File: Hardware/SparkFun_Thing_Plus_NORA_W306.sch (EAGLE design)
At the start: 72 parts, among them J1 THING_PLUS_LOGICAL, J2 LiPo, J3 QWIIC_RA, J4 MICRO-SDFRICTION, J5 USB-C, J6 SWD (DNP), Q1 3.1A/30V/105mΩ, Q2 MBT3904DW1T1, U1 UBLOX_NORA_W306, U3 XC6222B331MR-G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

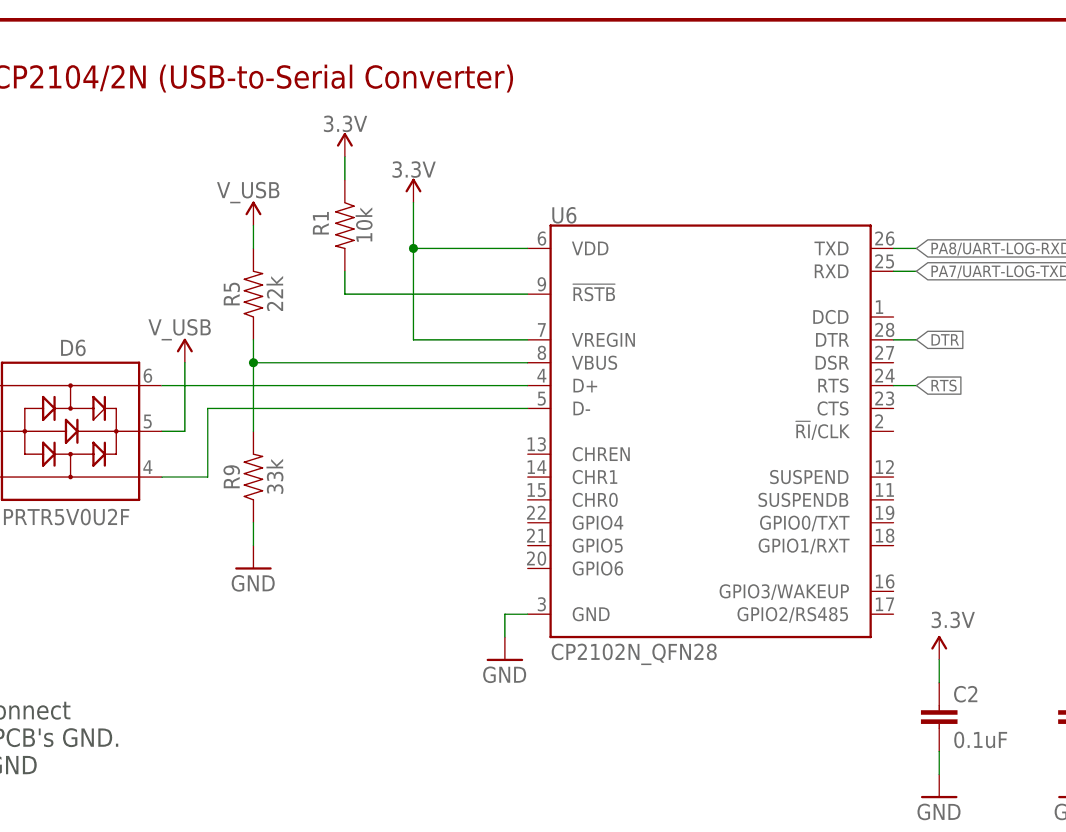
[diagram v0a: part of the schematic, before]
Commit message: Switched CP2102 to QFN24 package type
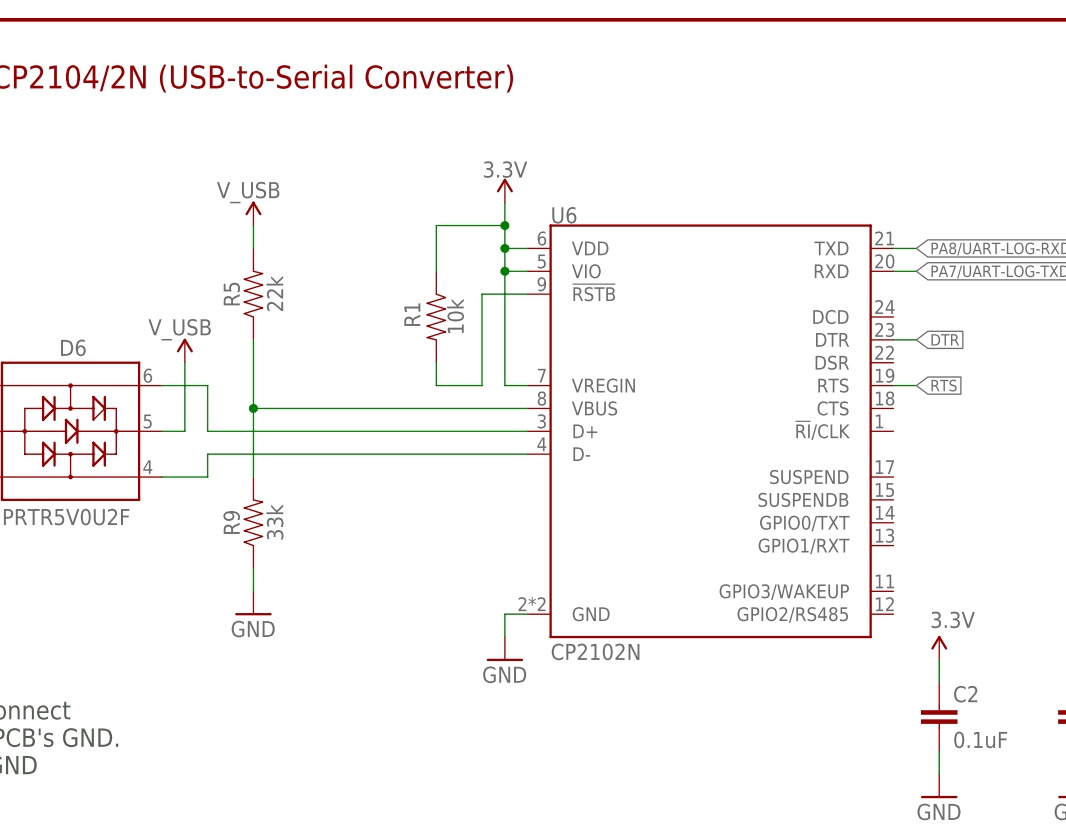
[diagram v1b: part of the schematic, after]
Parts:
- U6: value CP2102N_QFN28 -> CP2102N; device nora-w306:CP2102N_QFN28 -> SparkFun-IC-Comms:CP2102N
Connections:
- net 3.3V: now also U6.VIO
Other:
- moved on the sheet: R1, R9
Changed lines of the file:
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@@
 <part name="GND31" library="SparkFun-PowerSymbols" deviceset="GND" device=""/>
 <part name="CHG" library="SparkFun-Jumpers" deviceset="JUMPER-SMT_2_NC_TRACE" device="_SILK" package3d_urn="urn:adsk.eagle:package:39281/1" value=""/>
-<part name="U6" library="nora-w306" deviceset="CP2102N_QFN28" device=""/>
+<part name="U6" library="SparkFun-IC-Comms" deviceset="CP2102N" device=""/>
 <part name="GND32" library="SparkFun-PowerSymbols" deviceset="GND" device=""/>
-<part name="SUPPLY29" library="SparkFun-PowerSymbols" deviceset="3.3V" device=""/>
 <part name="JP3" library="SparkFun-Jumpers" deviceset="JUMPER-SMT_2_NC_TRACE" device="_SILK" package3d_urn="urn:adsk.eagle:package:39281/1" value=""/>
 <part name="I2C" library="SparkFun-Jumpers" deviceset="JUMPER-SMT_3_2-NC_TRACE" device="_SILK" package3d_urn="urn:adsk.eagle:package:39289/1"/>
@@
 <attribute name="VALUE" x="373.38" y="132.08" size="1.778" layer="96" font="vector"/>
 </instance>
-<instance part="R1" gate="G$1" x="340.36" y="256.54" smashed="yes" rot="R270">
-<attribute name="NAME" x="336.804" y="256.794" size="1.778" layer="95" font="vector" rot="R270" align="bottom-center"/>
-<attribute name="VALUE" x="343.408" y="256.54" size="1.778" layer="96" font="vector" rot="R270" align="top-center"/>
-</instance>
-<instance part="SUPPLY9" gate="G$1" x="347.98" y="259.08" smashed="yes">
-<attribute name="VALUE" x="347.98" y="261.874" size="1.778" layer="96" font="vector" align="bottom-center"/>
+<instance part="R1" gate="G$1" x="350.52" y="246.38" smashed="yes" rot="R270">
+<attribute name="NAME" x="346.964" y="246.634" size="1.778" layer="95" font="vector" rot="R270" align="bottom-center"/>
+<attribute name="VALUE" x="353.568" y="246.38" size="1.778" layer="96" font="vector" rot="R270" align="top-center"/>
+</instance>
+<instance part="SUPPLY9" gate="G$1" x="358.14" y="259.08" smashed="yes">
+<attribute name="VALUE" x="358.14" y="261.874" size="1.778" layer="96" font="vector" align="bottom-center"/>
 </instance>
 <instance part="SUPPLY3" gate="G$1" x="167.64" y="165.1" smashed="yes" rot="MR0">
@@
 <attribute name="VALUE" x="331.724" y="248.92" size="1.778" layer="96" font="vector" rot="R90" align="top-center"/>
 </instance>
-<instance part="R9" gate="G$1" x="330.2" y="228.6" smashed="yes" rot="R90">
-<attribute name="NAME" x="328.676" y="228.6" size="1.778" layer="95" font="vector" rot="R90" align="bottom-center"/>
-<attribute name="VALUE" x="331.724" y="228.6" size="1.778" layer="96" font="vector" rot="R90" align="top-center"/>
-</instance>
-<instance part="GND3" gate="1" x="330.2" y="218.44" smashed="yes">
-<attribute name="VALUE" x="327.66" y="215.9" size="1.778" layer="96" font="vector"/>
+<instance part="R9" gate="G$1" x="330.2" y="223.52" smashed="yes" rot="R90">
+<attribute name="NAME" x="328.676" y="223.52" size="1.778" layer="95" font="vector" rot="R90" align="bottom-center"/>
+<attribute name="VALUE" x="331.724" y="223.52" size="1.778" layer="96" font="vector" rot="R90" align="top-center"/>
+</instance>
+<instance part="GND3" gate="1" x="330.2" y="213.36" smashed="yes">
+<attribute name="VALUE" x="327.66" y="210.82" size="1.778" layer="96" font="vector"/>
 </instance>
 <instance part="C2" gate="G$1" x="406.4" y="200.66" smashed="yes">
@@
 <instance part="GND32" gate="1" x="358.14" y="208.28" smashed="yes">
 <attribute name="VALUE" x="355.6" y="205.74" size="1.778" layer="96" font="vector"/>
-</instance>
-<instance part="SUPPLY29" gate="G$1" x="340.36" y="264.16" smashed="yes">
-<attribute name="VALUE" x="340.36" y="266.954" size="1.778" layer="96" font="vector" align="bottom-center"/>
 </instance>
 <instance part="JP3" gate="G$1" x="170.18" y="60.96" smashed="yes">
@@
 </segment>
 <segment>
-<pinref part="SUPPLY29" gate="G$1" pin="3.3V"/>
+<pinref part="SUPPLY9" gate="G$1" pin="3.3V"/>
+<junction x="358.14" y="254"/>
+<wire x1="358.14" y1="238.76" x2="358.14" y2="251.46" width="0.1524" layer="91"/>
+<wire x1="358.14" y1="251.46" x2="358.14" y2="254" width="0.1524" layer="91"/>
+<wire x1="358.14" y1="254" x2="358.14" y2="256.54" width="0.1524" layer="91"/>
+<pinref part="U6" gate="G$1" pin="VDD"/>
+<wire x1="358.14" y1="256.54" x2="358.14" y2="259.08" width="0.1524" layer="91"/>
+<wire x1="358.14" y1="254" x2="360.68" y2="254" width="0.1524" layer="91"/>
+<pinref part="U6" gate="G$1" pin="VREGIN"/>
+<wire x1="358.14" y1="238.76" x2="360.68" y2="238.76" width="0.1524" layer="91"/>
 <pinref part="R1" gate="G$1" pin="1"/>
-<wire x1="340.36" y1="261.62" x2="340.36" y2="264.16" width="0.1524" layer="91"/>
-</segment>
-<segment>
-<pinref part="SUPPLY9" gate="G$1" pin="3.3V"/>
-<junction x="347.98" y="254"/>
-<wire x1="347.98" y1="243.84" x2="347.98" y2="254" width="0.1524" layer="91"/>
-<wire x1="347.98" y1="254" x2="347.98" y2="259.08" width="0.1524" layer="91"/>
-<pinref part="U6" gate="G$1" pin="VDD"/>
-<wire x1="347.98" y1="254" x2="360.68" y2="254" width="0.1524" layer="91"/>
-<pinref part="U6" gate="G$1" pin="VREGIN"/>
-<wire x1="347.98" y1="243.84" x2="360.68" y2="243.84" width="0.1524" layer="91"/>
+<wire x1="350.52" y1="251.46" x2="350.52" y2="256.54" width="0.1524" layer="91"/>
+<wire x1="358.14" y1="256.54" x2="350.52" y2="256.54" width="0.1524" layer="91"/>
+<junction x="358.14" y="256.54"/>
+<pinref part="U6" gate="G$1" pin="VIO"/>
+<wire x1="360.68" y1="251.46" x2="358.14" y2="251.46" width="0.1524" layer="91"/>
+<junction x="358.14" y="251.46"/>
 </segment>
 <segment>
@@
 <segment>
 <pinref part="R9" gate="G$1" pin="1"/>
-<wire x1="330.2" y1="223.52" x2="330.2" y2="220.98" width="0.1524" layer="91"/>
+<wire x1="330.2" y1="218.44" x2="330.2" y2="215.9" width="0.1524" layer="91"/>
 <pinref part="GND3" gate="1" pin="GND"/>
 </segment>
@@
 <segment>
 <pinref part="R1" gate="G$1" pin="2"/>
-<wire x1="340.36" y1="248.92" x2="340.36" y2="251.46" width="0.1524" layer="91"/>
+<wire x1="355.6" y1="238.76" x2="350.52" y2="238.76" width="0.1524" layer="91"/>
+<wire x1="350.52" y1="238.76" x2="350.52" y2="241.3" width="0.1524" layer="91"/>
 <pinref part="U6" gate="G$1" pin="!RSTB"/>
-<wire x1="340.36" y1="248.92" x2="360.68" y2="248.92" width="0.1524" layer="91"/>
+<wire x1="355.6" y1="238.76" x2="355.6" y2="248.92" width="0.1524" layer="91"/>
+<wire x1="355.6" y1="248.92" x2="360.68" y2="248.92" width="0.1524" layer="91"/>
 </segment>
 </net>
@@
 <pinref part="R9" gate="G$1" pin="2"/>
 <pinref part="R5" gate="G$1" pin="1"/>
-<wire x1="330.2" y1="233.68" x2="330.2" y2="241.3" width="0.1524" layer="91"/>
-<wire x1="330.2" y1="241.3" x2="330.2" y2="243.84" width="0.1524" layer="91"/>
-<junction x="330.2" y="241.3"/>
-<wire x1="360.68" y1="241.3" x2="330.2" y2="241.3" width="0.1524" layer="91"/>
+<wire x1="330.2" y1="228.6" x2="330.2" y2="236.22" width="0.1524" layer="91"/>
+<wire x1="330.2" y1="236.22" x2="330.2" y2="243.84" width="0.1524" layer="91"/>
+<junction x="330.2" y="236.22"/>
+<wire x1="360.68" y1="236.22" x2="330.2" y2="236.22" width="0.1524" layer="91"/>
 <pinref part="U6" gate="G$1" pin="VBUS"/>
 </segment>
@@
 <net name="N$15" class="0">
 <segment>
-<wire x1="360.68" y1="238.76" x2="320.04" y2="238.76" width="0.1524" layer="91"/>
+<wire x1="360.68" y1="233.68" x2="325.12" y2="233.68" width="0.1524" layer="91"/>
+<wire x1="325.12" y1="233.68" x2="325.12" y2="238.76" width="0.1524" layer="91"/>
+<wire x1="325.12" y1="238.76" x2="320.04" y2="238.76" width="0.1524" layer="91"/>
 <pinref part="D6" gate="D1" pin="6"/>
 <pinref part="U6" gate="G$1" pin="D+"/>
@@
 <net name="N$18" class="0">
 <segment>
-<wire x1="360.68" y1="236.22" x2="325.12" y2="236.22" width="0.1524" layer="91"/>
-<wire x1="325.12" y1="236.22" x2="325.12" y2="228.6" width="0.1524" layer="91"/>
+<wire x1="360.68" y1="231.14" x2="325.12" y2="231.14" width="0.1524" layer="91"/>
+<wire x1="325.12" y1="231.14" x2="325.12" y2="228.6" width="0.1524" layer="91"/>
 <wire x1="325.12" y1="228.6" x2="320.04" y2="228.6" width="0.1524" layer="91"/>
 <pinref part="D6" gate="D1" pin="4"/>

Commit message: Rerouted with new pin selections
-SPI0 now used for "main" SPI headers and uSD
-SPI1 PICO pin used for WS2812 control
-RX1/TX1 pins changed to other option on module
-I2C pins changed to other option on module
-SWD lines routed to DNP header on bottom side.
-most GPIOs switched/rerouted *note, Arduino pin map table not yet updated*
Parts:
- removed TP2: TEST-POINT3X5, SparkFun-Connectors:TEST-POINT3X5
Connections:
- removed net N$28: D5.DO, TP2.1
- removed net PA12/PICO: J1.PICO, J4.CMD/SDI, U1.PA12/LP_UART_TXD/SPI1_PICO/I2S_MCLK
- removed net PA13/POCI: J1.POCI, J4.DAT0/SDO, U1.PA13/LP_UART_RXD/SPI1_POCI/I2S_SD_TX1
- removed net PA14/SCK: J1.SCK, J4.CLK/SCK, U1.PA14/LP_UART_RTS/SPI1CLK/I2S_SD_TX2
- removed net PA15/CS: J1.A5, J4.DAT3/!CS!, U1.PA15/LP_UART_CTS/SPI1_CS
- removed net PA25/LP_UART_RXD: J1.RX, U1.PA25/HS_USI_SPI_PICO/HSDM/LP_UART_RXD
- removed net PA26/LP_UART_TXD: J1.TX, U1.PA26/HS_USI_SPI_POCI/HSDP/LP_UART_TXD
- removed net PB1: J1.A0, U1.PB1/LP_UART_TXD/ADC
- removed net PB18: J1.GPIO3, S3.1, S3.2, U1.PB18/HS_USI_USART0_RXD
- removed net PB19: J1.GPIO4, U1.PB19/HS_UART0_TXD/I2S_TX0
- removed net PB2: J1.A2, U1.PB2/LP_UART_RXD/PCM_CLK/ADC
- removed net PB20/SCL: J1.SCL, J3.4, R28.1, U1.PB20/HS_USI_I2C_SCL/I2S_CLK, U5.SCL
- removed net PB21/SDA: J1.SDA, J3.3, R29.1, U1.PB21/HS_USI_I2C_SDA/SPI0_CS/I2S_WS/QDEC_IDX, U5.SDA
- removed net PB3/ADC/SWD_CLK: J1.A1, J6.SWDCLK, U1.PB3/SWD_CLK/ADC
- new net PA12: J1.GPIO5, JP3.1, U1.PA12/LP_UART_TXD/SPI1_PICO/I2S_MCLK
- new net PA13: J1.GPIO6, U1.PA13/LP_UART_RXD/SPI1_POCI/I2S_SD_TX1
- new net PA14: J1.GPIO3, U1.PA14/LP_UART_RTS/SPI1_CLK/I2S_SD_TX2
- new net PA15: J1.GPIO4, U1.PA15/LP_UART_CTS/SPI1_CS
- new net PA25/SCL: J1.SCL, J3.4, R28.1, U1.PA25/LP_I2C_SCL/HSDM/LP_UART_RXD, U5.SCL
- new net PA26/SDA: J1.SDA, J3.3, R29.1, U1.PA26/LP_I2C_SDA/HSDP/LP_UART_TXD, U5.SDA
- new net PB1/LP_UART_TXD/A2: J1.TX, U1.PB1/LP_UART_TXD/ADC
- new net PB18/SPI0_PICO: J1.PICO, J4.CMD/SDI, U1.PB18/SPI0_PICO
- new net PB19/SPI0_POCI: J1.POCI, J4.DAT0/SDO, U1.PB19/SPI0_POCI/I2S_TX0
- new net PB2/LP_UART_RXD/A1: J1.RX, U1.PB2/LP_UART_RXD/PCM_CLK/ADC
- new net PB20/SPI0_CLK: J1.SCK, J4.CLK/SCK, U1.PB20/SPI0_CLK/I2S_CLK
- new net PB21/SPI0_CS: J1.A5, J4.DAT3/!CS!, U1.PB21/SPI0_CS/I2S_WS/QDEC_IDX
- new net PB3/SWD_CLK/A0: J1.A0, J6.SWDCLK, U1.PB3/SWD_CLK/ADC
- new net WS2812-DO: D5.DO, J1.GPIO0
- net PA28: now also J1.A4, U1.PA28/BT_CK/RREF; no longer J1.GPIO5, U1.PA28/HS_USI_SPI_CS/BT_CK/RREF
- net PA30: now also J1.A3, U1.PA30/HS_PWM7; no longer J1.GPIO6, U1.PA30/HS_USI_SPI_CLK/HS_PWM7
- net PA7/UART-LOG-TXD: now also J1.A2; no longer J1.A4
- net PA8/UART-LOG-RXD: now also J1.A1; no longer J1.A3
- net PB22: now also J1.GPIO1, JP4.1, S3.1, S3.2; no longer J1.GPIO2, JP3.1
- net PB23: now also J1.GPIO2; no longer J1.GPIO1, JP4.1
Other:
- note added: "Cut JP3 to disconnect mic data from GPIO pin."
- note removed: "Cut JP3 to disconnect mic data from D15"
- moved on the sheet: C8, U1

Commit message: Silk Labels updated
-and some minor layout tweaks
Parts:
- renumbered JP3 to JP1, JP4 to JP2
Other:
- note added: "***Boot Strap Pins*** (Include internal pull-ups) See DS PG 10 for more info. PA30 PB19/SWD_DATA PA7/UART-LOG-TXD"
- note removed: "***Boot Strap Pins*** (Include internal pull-ups) See DS PG 10 for more info. PA30 (D3/SCK) PB19/SWD_DATA (D13) PA7/UART-LOG-TXD (D1)"
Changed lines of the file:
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@@
 <part name="U6" library="SparkFun-IC-Comms" deviceset="CP2102N" device=""/>
 <part name="GND32" library="SparkFun-PowerSymbols" deviceset="GND" device=""/>
-<part name="JP3" library="SparkFun-Jumpers" deviceset="JUMPER-SMT_2_NC_TRACE" device="_SILK" package3d_urn="urn:adsk.eagle:package:39281/1" value=""/>
+<part name="JP1" library="SparkFun-Jumpers" deviceset="JUMPER-SMT_2_NC_TRACE" device="_SILK" package3d_urn="urn:adsk.eagle:package:39281/1" value=""/>
 <part name="I2C" library="SparkFun-Jumpers" deviceset="JUMPER-SMT_3_2-NC_TRACE" device="_SILK" package3d_urn="urn:adsk.eagle:package:39289/1"/>
 <part name="SUPPLY30" library="SparkFun-PowerSymbols" deviceset="3.3V" device=""/>
 <part name="R28" library="SparkFun-Resistors" deviceset="2.2KOHM" device="-0402T-1/16W-1%" value="2.2k"/>
 <part name="R29" library="SparkFun-Resistors" deviceset="2.2KOHM" device="-0402T-1/16W-1%" value="2.2k"/>
-<part name="JP4" library="SparkFun-Jumpers" deviceset="JUMPER-SMT_2_NC_TRACE" device="_SILK" package3d_urn="urn:adsk.eagle:package:39281/1" value=""/>
+<part name="JP2" library="SparkFun-Jumpers" deviceset="JUMPER-SMT_2_NC_TRACE" device="_SILK" package3d_urn="urn:adsk.eagle:package:39281/1" value=""/>
 <part name="C11" library="SparkFun-Capacitors" deviceset="0.1UF" device="-0402T-16V-10%" value="0.1uF"/>
 <part name="GND7" library="SparkFun-PowerSymbols" deviceset="GND" device=""/>
@@
 (Include internal pull-ups)
 See DS PG 10 for more info.
-PA30 (D3/SCK)
-PB19/SWD_DATA (D13)
-PA7/UART-LOG-TXD (D1)</text>
+PA30
+PB19/SWD_DATA
+PA7/UART-LOG-TXD</text>
 <text x="119.38" y="140.716" size="1.778" layer="97" font="vector" align="bottom-center">Arduino
 Pin Mapping</text>
@@
 <attribute name="VALUE" x="355.6" y="205.74" size="1.778" layer="96" font="vector"/>
 </instance>
-<instance part="JP3" gate="G$1" x="170.18" y="60.96" smashed="yes">
+<instance part="JP1" gate="G$1" x="170.18" y="60.96" smashed="yes">
 <attribute name="NAME" x="170.18" y="64.008" size="1.778" layer="95" font="vector" align="center"/>
 <attribute name="VALUE" x="170.18" y="57.912" size="1.778" layer="96" font="vector" align="center"/>
@@
 <attribute name="VALUE" x="423.164" y="142.24" size="1.778" layer="96" font="vector" rot="R90" align="top-center"/>
 </instance>
-<instance part="JP4" gate="G$1" x="299.72" y="27.94" smashed="yes">
+<instance part="JP2" gate="G$1" x="299.72" y="27.94" smashed="yes">
 <attribute name="NAME" x="299.72" y="30.988" size="1.778" layer="95" font="vector" align="center"/>
 <attribute name="VALUE" x="299.72" y="24.892" size="1.778" layer="96" font="vector" align="center"/>
@@
 <label x="162.56" y="60.96" size="1.27" layer="95" font="vector" rot="R180" xref="yes"/>
 <wire x1="165.1" y1="60.96" x2="162.56" y2="60.96" width="0.1524" layer="91"/>
-<pinref part="JP3" gate="G$1" pin="1"/>
+<pinref part="JP1" gate="G$1" pin="1"/>
 </segment>
 <segment>
@@
 <wire x1="294.64" y1="27.94" x2="292.1" y2="27.94" width="0.1524" layer="91"/>
 <label x="292.1" y="27.94" size="1.27" layer="95" font="vector" rot="R180" xref="yes"/>
-<pinref part="JP4" gate="G$1" pin="1"/>
+<pinref part="JP2" gate="G$1" pin="1"/>
 </segment>
 </net>
@@
 <segment>
 <pinref part="D5" gate="G$1" pin="DI"/>
-<pinref part="JP3" gate="G$1" pin="2"/>
+<pinref part="JP1" gate="G$1" pin="2"/>
 <wire x1="175.26" y1="60.96" x2="177.8" y2="60.96" width="0.1524" layer="91"/>
 </segment>
@@
 <segment>
 <pinref part="R4" gate="G$1" pin="1"/>
-<pinref part="JP4" gate="G$1" pin="2"/>
+<pinref part="JP2" gate="G$1" pin="2"/>
 <wire x1="304.8" y1="27.94" x2="307.34" y2="27.94" width="0.1524" layer="91"/>
 </segment>

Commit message: Corrected User button and STAT LED silk
-Moved button to Arduino "17"
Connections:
- net PB22: no longer S3.1, S3.2
- net PB23: now also S3.1, S3.2
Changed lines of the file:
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@@
-</segment>
-<segment>
-<pinref part="S3" gate="G$1" pin="1"/>
-<wire x1="256.54" y1="55.88" x2="254" y2="55.88" width="0.1524" layer="91"/>
-<pinref part="S3" gate="G$1" pin="2"/>
-<wire x1="256.54" y1="53.34" x2="254" y2="53.34" width="0.1524" layer="91"/>
-<wire x1="254" y1="53.34" x2="254" y2="55.88" width="0.1524" layer="91"/>
-<wire x1="251.46" y1="55.88" x2="254" y2="55.88" width="0.1524" layer="91"/>
-<junction x="254" y="55.88"/>
-<label x="251.46" y="55.88" size="1.27" layer="95" font="vector" rot="R180" xref="yes"/>
 </segment>
 <segment>
@@
 <pinref part="J1" gate="G$1" pin="GPIO2"/>
 </segment>
+<segment>
+<pinref part="S3" gate="G$1" pin="1"/>
+<wire x1="256.54" y1="55.88" x2="254" y2="55.88" width="0.1524" layer="91"/>
+<pinref part="S3" gate="G$1" pin="2"/>
+<wire x1="256.54" y1="53.34" x2="254" y2="53.34" width="0.1524" layer="91"/>
+<wire x1="254" y1="53.34" x2="254" y2="55.88" width="0.1524" layer="91"/>
+<wire x1="251.46" y1="55.88" x2="254" y2="55.88" width="0.1524" layer="91"/>
+<junction x="254" y="55.88"/>
+<label x="251.46" y="55.88" size="1.27" layer="95" font="vector" rot="R180" xref="yes"/>
+</segment>
 </net>
